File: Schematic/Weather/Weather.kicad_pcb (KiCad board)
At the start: 2 copper layers, 131 parts, among them J1 4_Way_Wire, J10 Conn_02x04_Odd_Even, J11 Conn_01x04_Female, J12 Conn_01x05_Female, J13 Conn_01x04_Male, J14 Conn_01x05_Male, J15 Conn_02x04_Odd_Even, J2 3_Way_Wire, J3 3_Way_Wire, J4 3_Way_Wire, J5 3_Way_Wire, J6 3_Way_Wire, J7 3_Way_Wire, J8 3_Way_Wire, J9 3_Way_Wire, Q1 BSS138, Q10 BSS138, Q11 AO3401, Q12 AO3401, Q2 AO3401, Q3 AO3401, Q4 BSS138, Q5 AO3401, Q6 AO3401, Q7 BSS138, Q8 AO3401, Q9 AO3401, U1 AMS1117, U2 ESP-01v090, U3 AMS1117, U4 ESP-01v090, U5 LM321, U6 LM321, U7 LM321, U8 LM321

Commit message: more changes
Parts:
- removed the J11 at (61.4, -190.2)
- removed the J12 at (52.1, -190.2)
- added H1: MountingHole_Pad, Connector_Wire:SolderWirePad_1x01_Drill0.8mm, F.Cu at (176.5, -200.7)
- added H2: MountingHole_Pad, Connector_Wire:SolderWirePad_1x01_Drill0.8mm, F.Cu at (172.5, -200.7)
- added J14: 5_Way_Wire, Connector_PinHeader_2.54mm:PinHeader_1x05_P2.54mm_Vertical, F.Cu at (129.0, -209.7)
- added J15: 5_Way_Wire, Connector_PinHeader_2.54mm:PinHeader_1x05_P2.54mm_Vertical, F.Cu at (115.0, -209.7)
- added J16: 5_Way_Wire, Connector_PinHeader_2.54mm:PinHeader_1x05_P2.54mm_Vertical, F.Cu at (124.3, -209.7)
- added J17: 4_Way_Wire, Connector_PinHeader_2.54mm:PinHeader_1x04_P2.54mm_Vertical, F.Cu at (133.6, -209.7)
- added J18: 5_Way_Wire, Connector_PinHeader_2.54mm:PinHeader_1x05_P2.54mm_Vertical, F.Cu at (119.7, -209.7)
- added J24: Conn_01x05_Female, Connector_PinHeader_2.54mm:PinHeader_1x05_P2.54mm_Vertical, F.Cu at (151.9, -231.8)
- added J25: Conn_01x04_Female, Connector_PinHeader_2.54mm:PinHeader_1x05_P2.54mm_Vertical, F.Cu at (156.6, -231.8)
- added J26: Conn_01x04_Male, Connector_PinHeader_2.54mm:PinHeader_1x04_P2.54mm_Vertical, F.Cu at (128.9, -231.8)
- added J3: 3_Way_Wire, Connector_PinHeader_2.54mm:PinHeader_1x03_P2.54mm_Vertical, F.Cu at (172.8, -213.2)
- added J5: 4_Way_Wire, Connector_PinHeader_2.54mm:PinHeader_1x04_P2.54mm_Vertical, F.Cu at (182.7, -231.8)
- added J6: 4_Way_Wire, Connector_PinHeader_2.54mm:PinHeader_1x04_P2.54mm_Vertical, F.Cu at (187.3, -231.8)
- added J7: 4_Way_Wire, Connector_PinHeader_2.54mm:PinHeader_1x04_P2.54mm_Vertical, F.Cu at (115.0, -190.7)
- added J8: 4_Way_Wire, Connector_PinHeader_2.54mm:PinHeader_1x04_P2.54mm_Vertical, F.Cu at (153.1, -190.7)
- added MOD3: BMP180, footprint:BMP180, F.Cu at (117.1, -232.3)
- J13: value Conn_01x04_Male -> 3_Way_Wire; footprint Connector_PinHeader_2.54mm:PinHeader_1x04_P2.54mm_Vertical -> Connector_PinHeader_2.54mm:PinHeader_1x03_P2.54mm_Vertical
- MOD2: value BMP180 -> HTU21; footprint footprint:BMP180 -> footprint:HTU21
- moved MOD1 88.2 mm to (148.6, -210.2), turned to 0 degrees
- moved MOD2 80.9 mm to (143.9, -191.2), turned to 0 degrees
- moved J13 74.8 mm to (138.3, -209.7)
- moved U1 49.9 mm to (45.7, -135.9)
- moved J1 47.2 mm to (50.8, -139.7)
- turned U3 to 270 degrees
- renumbered C4 to C1, C5 to C2, C6 to C3, C7 to C4, C1 to C5, C2 to C6, C3 to C7, H8 to H10, H9 to H11, H10 to H12, H11 to H13, H12 to H14, H13 to H15, H14 to H16, H15 to H17, H16 to H18, H17 to H19, H18 to H20, H1 to H3, H2 to H4, H3 to H5, H4 to H6, H5 to H7, H6 to H8, H7 to H9, J10 to J1, J3 to J10, J4 to J11, J5 to J12, J6 to J19, J14 to J2, J7 to J20, J8 to J21, J9 to J22, J15 to J23, J1 to J4, J2 to J9, R3 to R1, R12 to R10, R13 to R11, R14 to R12, R15 to R13, R16 to R14, R17 to R15, R18 to R16, R19 to R17, R20 to R18, R21 to R19, R4 to R2, R22 to R20, R23 to R21, R24 to R22, R25 to R23, R26 to R24, R27 to R25, R28 to R26, R29 to R27, R30 to R28, R31 to R29, R5 to R3, R32 to R30, R33 to R31, R34 to R32, R35 to R33, R36 to R34, R37 to R35, R38 to R36, R39 to R37, R40 to R38, R41 to R39, R6 to R4, R42 to R40, R43 to R41, R44 to R42, R45 to R43, R46 to R44, R47 to R45, R48 to R46, R49 to R47, R50 to R48, R51 to R49, R7 to R5, R52 to R50, R53 to R51, R54 to R52, R55 to R53, R56 to R54, R57 to R55, R58 to R56, R1 to R57, R2 to R58, R8 to R6, R9 to R7, R10 to R8, R11 to R9, U2 to U1, U3 to U2, U4 to U3, U5 to U4, U6 to U5, U7 to U6, U8 to U7, U1 to U8
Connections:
- C5 pad 1: /Int Motherboard/J2_P2 -> /Int Motherboard/J17_P1
- C5 pad 2: /Int Motherboard/J2_P1 -> GND
- C6 pad 2: /Int Motherboard/J2_P1 -> GND
- C7 pad 2: /Int Motherboard/J2_P1 -> GND
- H19 pad 1: /Int Motherboard/J2_P2 -> /Int Motherboard/J17_P1
- H20 pad 1: /Int Motherboard/J2_P1 -> GND
- J1 pad 1: Net-(J10-Pad1) -> Net-(J1-Pad1)
- J1 pad 8: Net-(J10-Pad8) -> Net-(J1-Pad8)
- J13 pad 1: Net-(J13-Pad1) -> (no net)
- J13 pad 2: Net-(J13-Pad2) -> (no net)
- J13 pad 3: Net-(J13-Pad3) -> (no net)
- J2 pad 1: Net-(J14-Pad1) -> (no net)
- J2 pad 2: Net-(J14-Pad2) -> (no net)
- J2 pad 3: Net-(J14-Pad3) -> (no net)
- J2 pad 4: Net-(J14-Pad4) -> (no net)
- J2 pad 5: Net-(J14-Pad5) -> (no net)
- J23 pad 1: Net-(J15-Pad1) -> (no net)
- J23 pad 2: /Int Motherboard/J2_P1 -> GND
- J23 pad 4: /Int Motherboard/J3_P3 -> /Int Motherboard/J17_P3
- J23 pad 8: Net-(J15-Pad8) -> (no net)
- PSU1 pad 1: (no net) -> GND
- PSU1 pad 2: (no net) -> /Int Motherboard/J17_P1
- R57 pad 2: (no net) -> /Int Motherboard/J3_P4
- R58 pad 2: (no net) -> /Int Motherboard/J3_P2
- U1 pad 1: (no net) -> Net-(J1-Pad1)
- U1 pad 2: (no net) -> /Internal ESP8266/J3_P1
- U1 pad 3: (no net) -> /Internal ESP8266/J3_P2
- U1 pad 4: (no net) -> /Internal ESP8266/J3_P3
- U1 pad 5: (no net) -> /Internal ESP8266/J3_P4
- U1 pad 6: (no net) -> /Internal ESP8266/J3_P5
- U1 pad 7: (no net) -> /Internal ESP8266/J3_P6
- U1 pad 8: (no net) -> Net-(J1-Pad8)
- U8 pad 1: /Int Motherboard/J2_P1 -> GND
- U8 pad 3: /Int Motherboard/J2_P2 -> /Int Motherboard/J17_P1

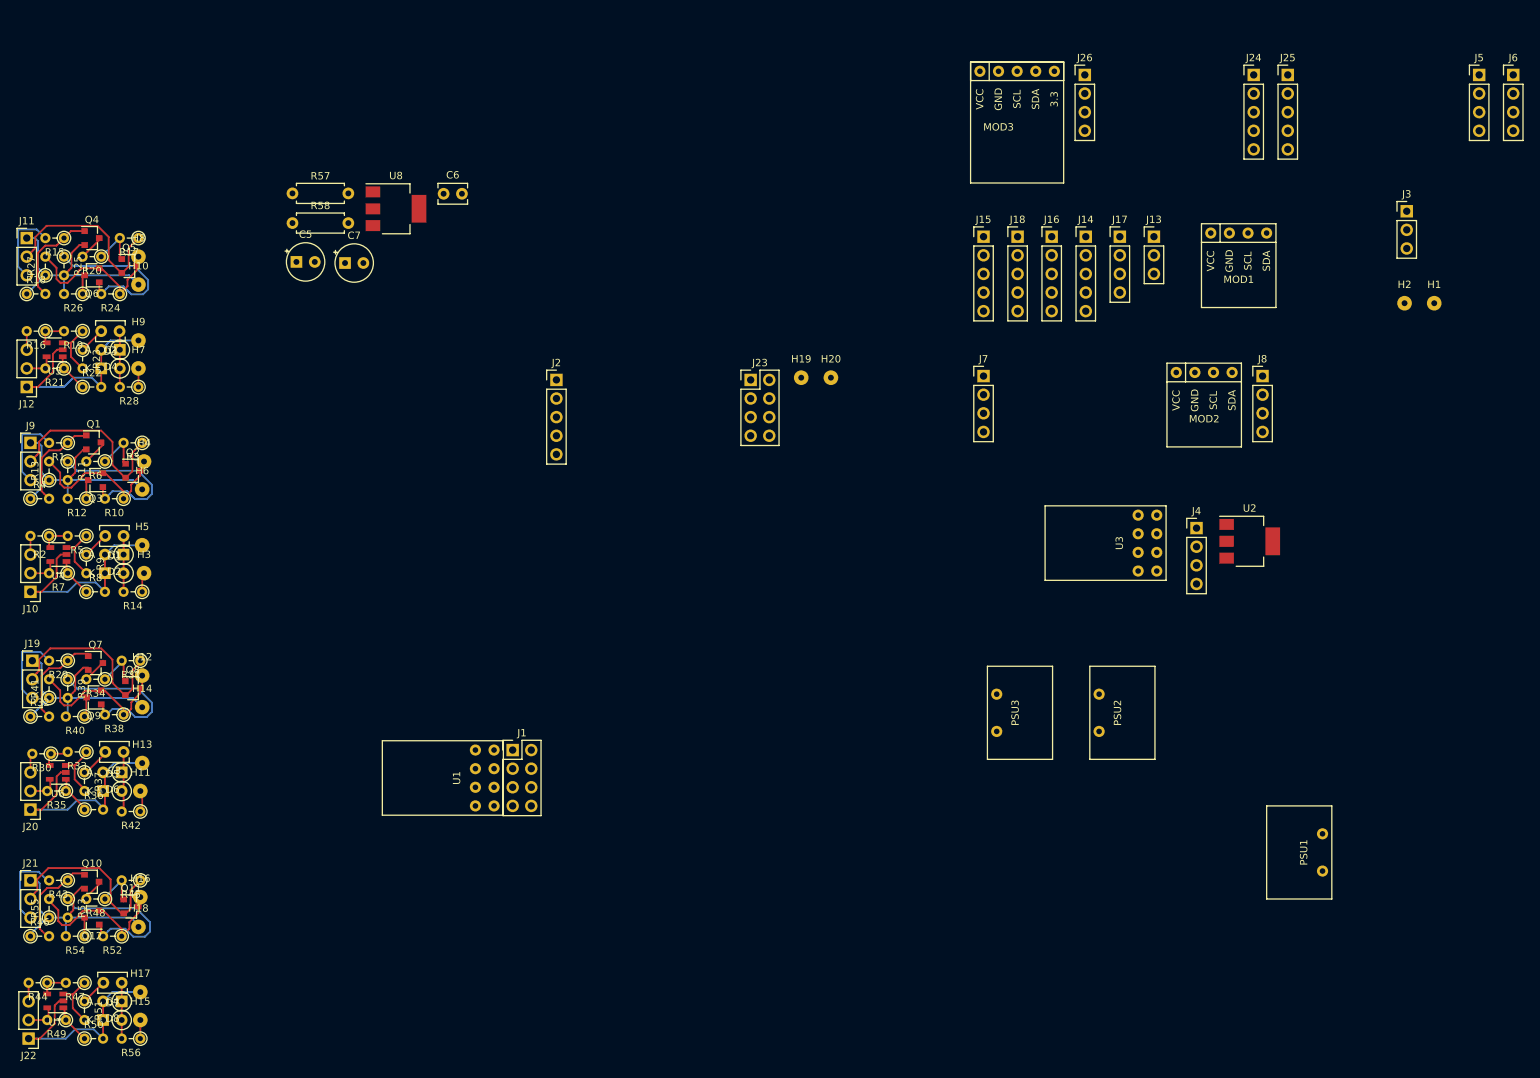
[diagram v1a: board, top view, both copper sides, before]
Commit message: Local webpage added
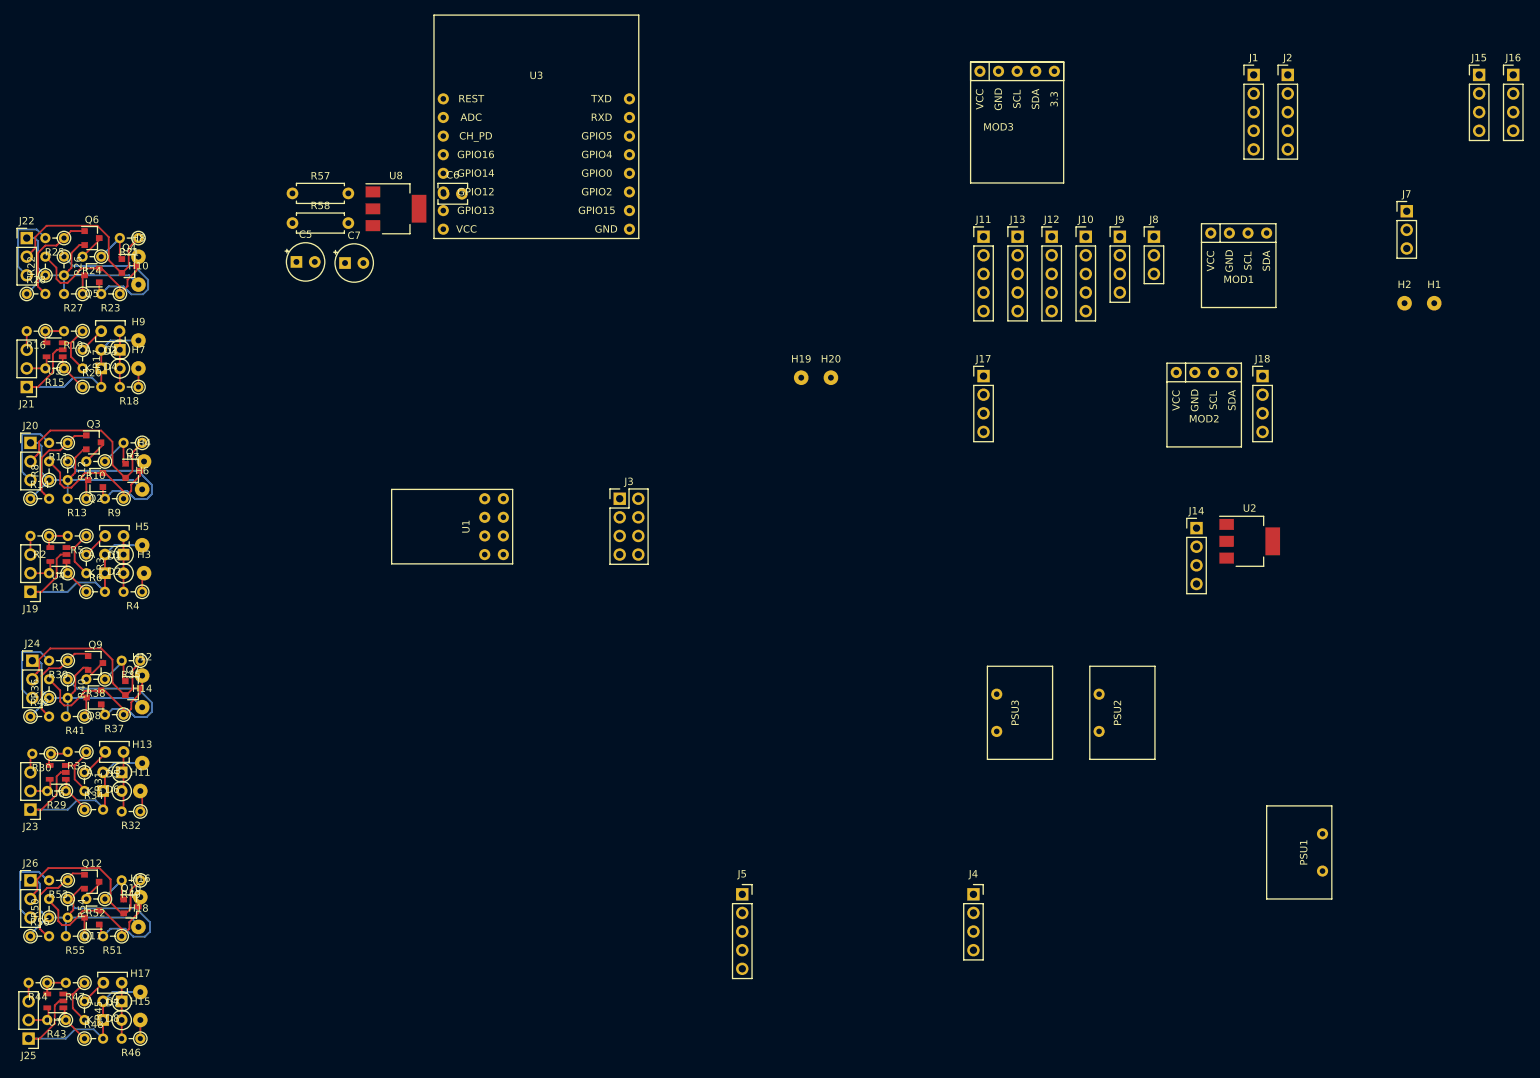
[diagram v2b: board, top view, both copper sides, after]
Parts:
- removed the J1 at (50.8, -139.7)
- removed the J2 at (56.8, -190.2)
- removed the J23 at (83.3, -190.2)
- removed the J26 at (128.9, -231.8)
- added J3: Conn_02x04_Odd_Even, Connector_PinHeader_2.54mm:PinHeader_2x04_P2.54mm_Vertical, F.Cu at (65.4, -174.0)
- added J4: 4_Way_Wire, Connector_PinSocket_2.54mm:PinSocket_1x04_P2.54mm_Vertical, F.Cu at (113.7, -120.0)
- added J5: 5_Way_Wire, Connector_PinSocket_2.54mm:PinSocket_1x05_P2.54mm_Vertical, F.Cu at (82.1, -120.0)
- U3: value ESP-01v090 -> ESP-12; footprint footprint:ESP-01 -> footprint:ESP-12_breakout
- moved U3 100.2 mm to (54.0, -225.4), turned to 0 degrees
- moved U1 34.3 mm to (47.0, -170.2)
- renumbered J24 to J1, J14 to J10, J15 to J11, J16 to J12, J18 to J13, J4 to J14, J5 to J15, J6 to J16, J7 to J17, J8 to J18, J10 to J19, J25 to J2, J9 to J20, J12 to J21, J11 to J22, J20 to J23, J19 to J24, J22 to J25, J21 to J26, J3 to J7, J13 to J8, J17 to J9, Q2 to Q1, Q11 to Q10, Q12 to Q11, Q10 to Q12, Q3 to Q2, Q1 to Q3, Q5 to Q4, Q6 to Q5, Q4 to Q6, Q8 to Q7, Q9 to Q8, Q7 to Q9, R7 to R1, R6 to R10, R1 to R11, R11 to R12, R12 to R13, R4 to R14, R21 to R15, R23 to R17, R28 to R18, R22 to R20, R17 to R21, R27 to R22, R24 to R23, R20 to R24, R15 to R25, R25 to R26, R26 to R27, R18 to R28, R35 to R29, R9 to R3, R37 to R31, R42 to R32, R36 to R34, R31 to R35, R41 to R36, R38 to R37, R34 to R38, R29 to R39, R14 to R4, R39 to R40, R40 to R41, R32 to R42, R49 to R43, R51 to R45, R56 to R46, R50 to R48, R45 to R49, R55 to R50, R52 to R51, R48 to R52, R43 to R53, R53 to R54, R54 to R55, R46 to R56, R8 to R6, R3 to R7, R13 to R8, R10 to R9
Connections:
- net /Anenometer Control Board/J14_P2 renamed /Anenometer Control Board/J11_P2
- net /Anenometer Control Board/J14_P3 renamed /Anenometer Control Board/J11_P3
- net /Anenometer Control Board/J14_P4 renamed /Anenometer Control Board/J11_P4
- net /Anenometer Control Board/J14_P5 renamed /Anenometer Control Board/J11_P5
- net /Eath Sensor/J19_P1 renamed /Anenometer Control Board/J12_P1
- net /Eath Sensor/J19_P2 renamed /Anenometer Control Board/J12_P2
- net /Eath Sensor/J19_P3 renamed /Anenometer Control Board/J12_P3
- net /Eath Sensor/J19_P4 renamed /Anenometer Control Board/J12_P5
- net /Eath Sensor/J19_P5 renamed /Anenometer Control Board/J12_P4
- net /North Sensor/J17_P1 renamed /Anenometer Control Board/J10_P1
- net /North Sensor/J17_P2 renamed /Anenometer Control Board/J10_P2
- net /North Sensor/J17_P3 renamed /Anenometer Control Board/J10_P3
- net /North Sensor/J17_P4 renamed /Anenometer Control Board/J10_P4
- net /North Sensor/J17_P5 renamed /Anenometer Control Board/J10_P5
- net /West Sensor/J20_P1 renamed /Anenometer Control Board/J13_P1
- net /West Sensor/J20_P2 renamed /Anenometer Control Board/J13_P2
- net /West Sensor/J20_P3 renamed /Anenometer Control Board/J13_P3
- net /West Sensor/J20_P4 renamed /Anenometer Control Board/J13_P4
- net /West Sensor/J20_P5 renamed /Anenometer Control Board/J13_P5
- C5 pad 1: /Int Motherboard/J17_P1 -> /Int Motherboard/J0_P2
- H1 pad 1: /Int Motherboard/J17_P1 -> /Int Motherboard/J0_P2
- H19 pad 1: /Int Motherboard/J17_P1 -> /Int Motherboard/J0_P2
- J1 pad 1: (no net) -> GND
- J1 pad 2: (no net) -> /Int Motherboard/J1_P2
- J1 pad 3: (no net) -> /Int Motherboard/J1_P3
- J1 pad 4: (no net) -> /Int Motherboard/J0_P2
- J14 pad 1: (no net) -> /External ESP8266/J14_P1
- J14 pad 2: (no net) -> /External ESP8266/J14_P2
- J14 pad 3: (no net) -> /External ESP8266/J14_P3
- J14 pad 4: (no net) -> /External ESP8266/J14_P4
- J15 pad 1: (no net) -> /External ESP8266/J14_P1
- J15 pad 2: (no net) -> /External ESP8266/J14_P2
- J15 pad 3: (no net) -> /External ESP8266/J14_P3
- J15 pad 4: (no net) -> /External ESP8266/J14_P4
- J16 pad 1: (no net) -> /External ESP8266/J14_P1
- J16 pad 2: (no net) -> /External ESP8266/J14_P2
- J16 pad 3: (no net) -> /External ESP8266/J14_P3
- J16 pad 4: (no net) -> /External ESP8266/J14_P4
- J17 pad 1: (no net) -> /External ESP8266/J14_P1
- J17 pad 2: (no net) -> /External ESP8266/J14_P2
- J17 pad 3: (no net) -> /External ESP8266/J14_P3
- J17 pad 4: (no net) -> /External ESP8266/J14_P4
- J18 pad 1: (no net) -> /External ESP8266/J14_P1
- J18 pad 2: (no net) -> /External ESP8266/J14_P2
- J18 pad 3: (no net) -> /External ESP8266/J14_P3
- J18 pad 4: (no net) -> /External ESP8266/J14_P4
- J2 pad 1: /Int Motherboard/J17_P1 -> GND
- J2 pad 2: GND -> /Int Motherboard/J1_P2
- J2 pad 3: /Int Motherboard/J17_P3 -> /Int Motherboard/J1_P3
- J2 pad 4: /Int Motherboard/J3_P5 -> /Int Motherboard/J0_P2
- J7 pad 1: (no net) -> /PSU 2/J7_P1
- J7 pad 2: (no net) -> /PSU 2/J7_P2
- J7 pad 3: (no net) -> /PSU 2/J7_P3
- MOD1 pad 1: (no net) -> GND
- MOD1 pad 2: (no net) -> /Int Motherboard/J1_P2
- MOD1 pad 3: (no net) -> /Int Motherboard/J1_P3
- MOD1 pad 4: (no net) -> /Int Motherboard/J0_P2
- MOD2 pad 1: (no net) -> /External ESP8266/J14_P1
- MOD2 pad 2: (no net) -> /External ESP8266/J14_P2
- MOD2 pad 3: (no net) -> /External ESP8266/J14_P3
- MOD2 pad 4: (no net) -> /External ESP8266/J14_P4
- MOD3 pad 1: (no net) -> /Int Motherboard/J0_P2
- MOD3 pad 2: (no net) -> GND
- MOD3 pad 3: (no net) -> /Int Motherboard/J1_P2
- MOD3 pad 4: (no net) -> /Int Motherboard/J1_P3
- PSU1 pad 2: /Int Motherboard/J17_P1 -> /Int Motherboard/J0_P2
- PSU2 pad 1: /PSU 2/J5_P1 -> /PSU 2/J7_P2
- PSU2 pad 2: (no net) -> /PSU 2/J7_P1
- PSU3 pad 1: /PSU 2/J5_P1 -> /PSU 2/J7_P2
- PSU3 pad 2: (no net) -> /PSU 2/J7_P3
- R57 pad 2: /Int Motherboard/J3_P4 -> /Int Motherboard/J1_P3
- R58 pad 2: /Int Motherboard/J3_P2 -> /Int Motherboard/J1_P2
- U1 pad 2: /Internal ESP8266/J3_P1 -> GND
- U1 pad 3: /Internal ESP8266/J3_P2 -> /Int Motherboard/J1_P2
- U1 pad 4: /Internal ESP8266/J3_P3 -> /Int Motherboard/J3_P3
- U1 pad 5: /Internal ESP8266/J3_P4 -> /Int Motherboard/J1_P3
- U1 pad 6: /Internal ESP8266/J3_P5 -> /Int Motherboard/J3_P5
- U1 pad 7: /Internal ESP8266/J3_P6 -> /Int Motherboard/J3_P6
- U2 pad 1: Net-(U2-Pad1) -> /External ESP8266/J14_P1
- U2 pad 3: (no net) -> /External ESP8266/J14_P4
- U3 pad 2: Net-(U2-Pad1) -> (no net)
- U3 pad 6: (no net) -> /External ESP8266/J14_P2
- U3 pad 7: Net-(U2-Pad2) -> /External ESP8266/J14_P3
- U3 pad 8: (no net) -> Net-(U2-Pad2)
- U8 pad 3: /Int Motherboard/J17_P1 -> /Int Motherboard/J0_P2
